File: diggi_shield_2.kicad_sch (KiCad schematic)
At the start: 100 parts, among them J1_P1 IN_L, J1_P2 IN_GND, J1_P3 IN_R, J1_P4 OUT_R, J1_P5 OUT_GND, J1_P6 OUT_L, J2_P1 HP_R, J2_P2 HP_GND, J2_P3 HP_L, J8_P1 GND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

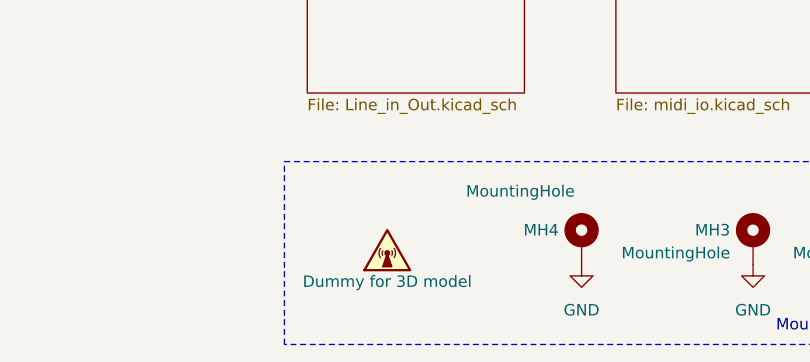
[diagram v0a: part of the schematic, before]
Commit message: Removed final warnings
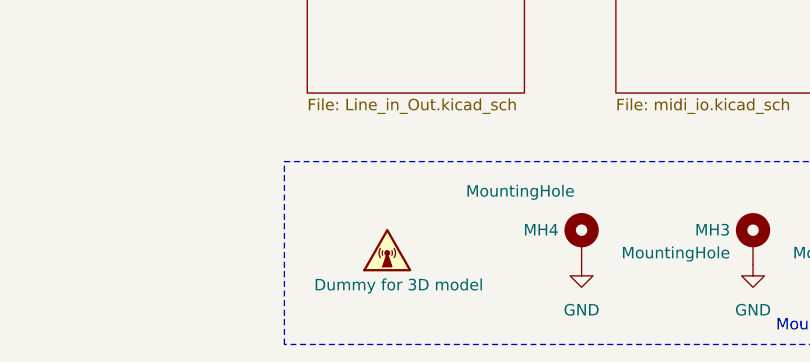
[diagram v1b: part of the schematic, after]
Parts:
- DUMMY1: now left out of the parts list
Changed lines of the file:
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@@
 		(unit 1)
 		(exclude_from_sim no)
-		(in_bom yes)
-		(on_board yes)
+		(in_bom no)
+		(on_board no)
 		(dnp no)
-		(fields_autoplaced yes)
 		(property "Reference" "DUMMY1"
 			(at 24.13 183.134 0)
@@
 		)
 		(property "Value" "Dummy for 3D model"
-			(at 24.13 189.865 0)
+			(at 16.002 190.246 0)
 			(effects
 				(font
 					(size 1.27 1.27)
 				)
+				(justify left)
 			)
 		)
@@
 			)
 		)
-		(property "Description" ""
+		(property "Description" "Radio waves warning symbol, small"
 			(at 24.13 186.69 0)
 			(effects
@@
 					(size 1.27 1.27)
 				)
+				(hide yes)
 			)
 		)
+		(property "Sim.Enable" "0"
+			(at 24.13 186.69 0)
+			(effects
+				(font
+					(size 1.27 1.27)
+				)
+				(hide yes)
+			)
+		)
